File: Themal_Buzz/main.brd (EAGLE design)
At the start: 42.5 x 32.1 mm, 12 parts

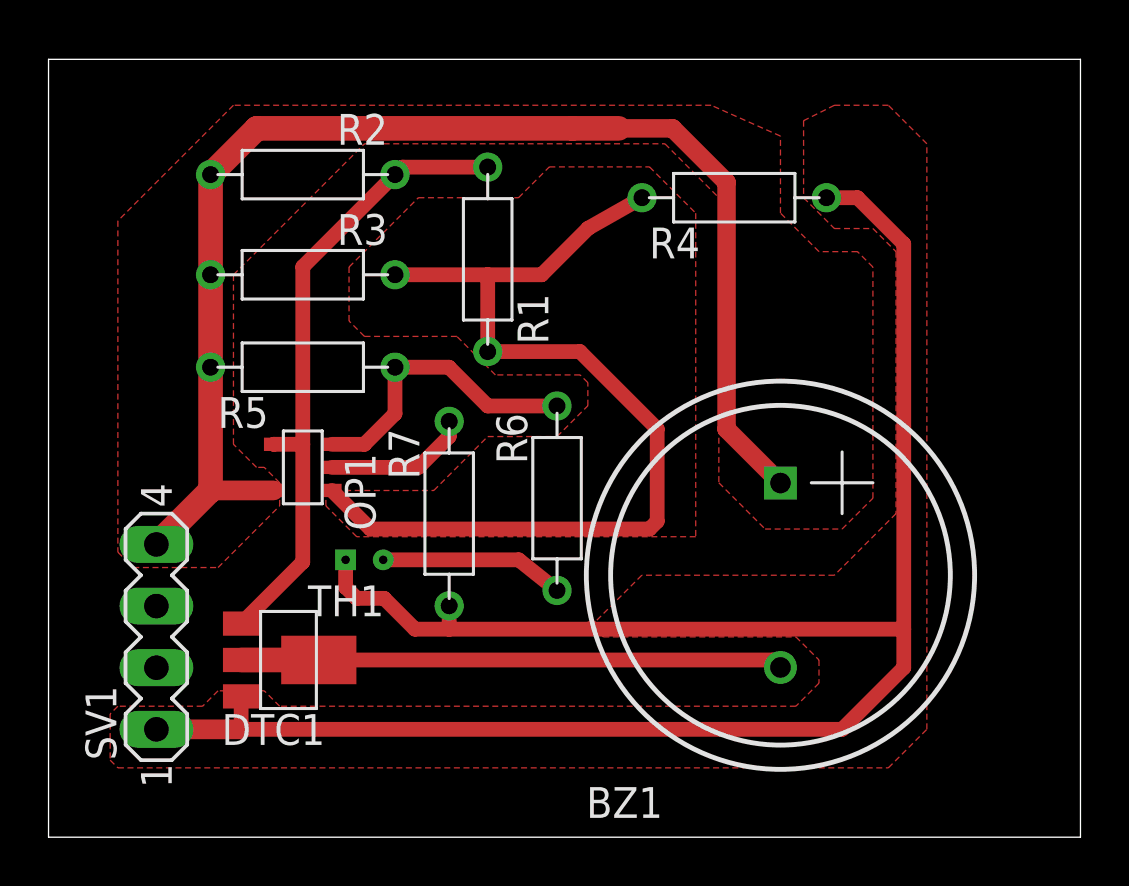
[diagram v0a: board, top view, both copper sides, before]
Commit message: 抵抗値の設定完了
各抵抗値の設定完了
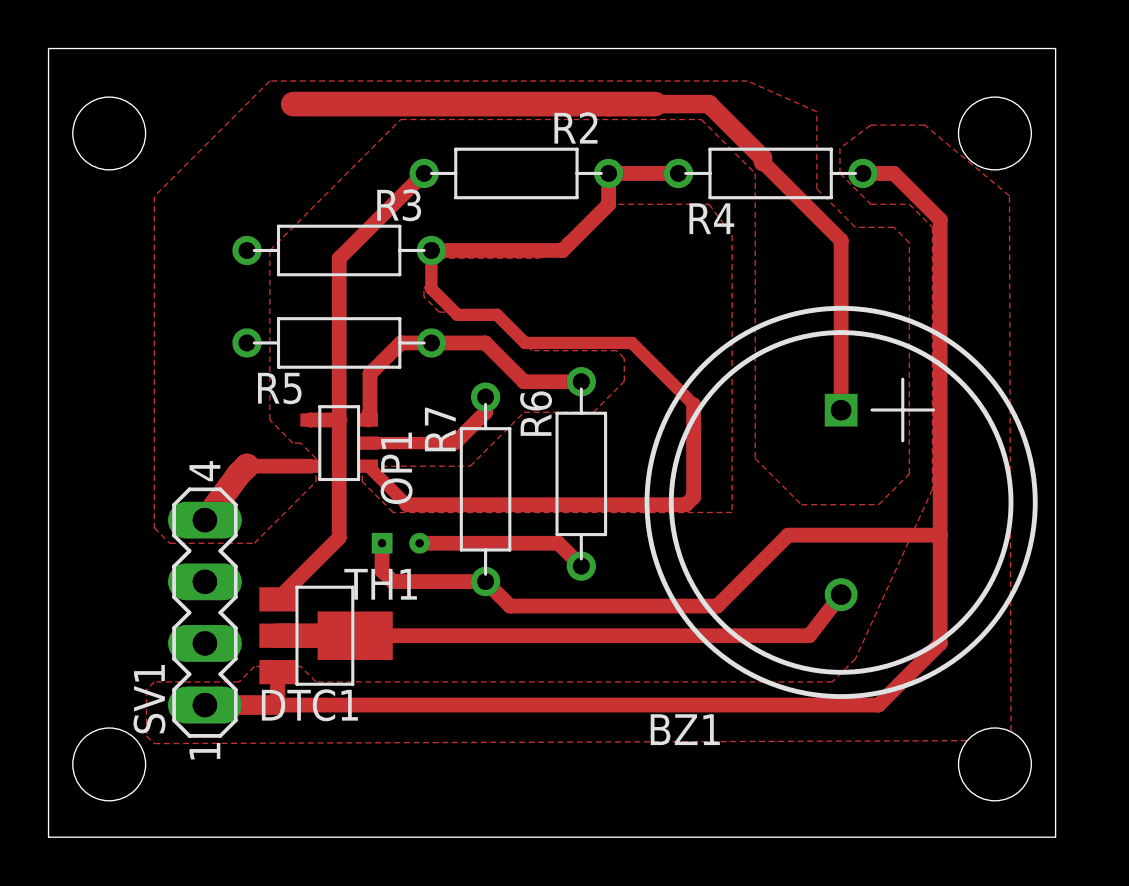
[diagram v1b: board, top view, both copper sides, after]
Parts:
- removed R1: 1/4W_RESISTER, Tr_EXT:MF1/4
- R2: value 1/4W_RESISTER -> 39KΩ
- R3: value 1/4W_RESISTER -> 18KΩ
- R4: value 1/4W_RESISTER -> 120KΩ
- R5: value 1/4W_RESISTER -> 1KΩ
- moved R2 8.80 mm to (19.3, 27.4)
- moved BZ1 3.91 mm to (32.7, 13.8)
- moved SV1 2.24 mm to (6.45, 9.26)
- moved DTC1 1.80 mm to (9.44, 8.30)
- moved R3 1.80 mm to (12.0, 24.2)
- moved R4 1.80 mm to (29.8, 27.4)
- moved R5 1.80 mm to (12.0, 20.4)
- moved R7 1.80 mm to (18.0, 14.3)
- moved OP1 1.80 mm to (12.0, 16.2)
- moved TH1 1.65 mm to (14.5, 12.1)
- moved R6 1.41 mm to (22.0, 15.0)
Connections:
- removed net N$3: OP1.P$1, R1.P$1, R3.P$1, R4.P$1
- new net N$7: OP1.P$1, R2.P$1, R3.P$1, R4.P$1
- net N$1: now also R2.P$2; no longer R1.P$2, R2.P$1
- net VCC: no longer R2.P$2
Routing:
- net N$7: track 0.00 -> 44.6 mm
- net N$3: track 40.8 -> 0.00 mm
- net VCC: track 57.0 -> 39.8 mm
- net N$1: track 26.3 -> 21.3 mm
- net N$4: track 22.8 -> 24.5 mm
- net N$5: track 7.60 -> 7.05 mm
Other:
- board size 42.5 x 32.1 mm -> 41.5 x 32.5 mm
